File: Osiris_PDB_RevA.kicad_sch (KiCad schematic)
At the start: 69 parts, among them J1 MKDSP 25/2-15.00, J2 OSIRIS_I2C, J3 MKDSP 25/2-15.00, J4 XT60PW-F, Q1 ISC015N06NM5LF2, Q2 ISC015N06NM5LF2, Q3 BSC070N10NS5, U1 LTC4368HMS-1-PBF, U2 INA228AIDGSR, U3 LT3010EMS8E, U4 74AUP1G07GW, U5 LTC4359IMS8

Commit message: Update REV1.1 XT60 PDB and publish clean JLCPCB outputs
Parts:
- C17: value 470u 35V HYBRID -> 330u 50V HYBRID; MPN EEHZS1V471P -> EEHZL1H331P; Selection_Status Selected EEHZS1V471P G16; 10 mm diameter, 16.5 mm height. A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 -> Voltage rating increased to 50 V; same G16 footprint. Nomin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
- D5: value SMBJ24CA -> SMBJ18CA; MPN SMBJ24CA -> SMBJ18CA; Selection_Status SMBJ24CA retained for local ringing control. Clamp is not a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 -> Selected for confirmed 4S 16.8 V supply and 50 V C17. Clamp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
- J1, J3: value MKDSP 25/2-15.00 -> XT60PW-F; footprint PDB_Footprints:Connector_MKDSP25_2_15mm -> PDB_Footprints:AMASS_XT60PW-F_1x02_P7.20mm_Horizontal_EdgeMounted; symbol PDB_Symbols:Conn_01x02_Phoenix -> PDB_Symbols:XT60PW_F; MPN 1932588 -> XT60PW-F; Manufacturer Phoenix Contact -> AMASS; Selection_Status Drawing checked 2026-10-01: 15 mm pole pitch, 3.8 mm paired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 -> XT60PW-F rated 45 A, momentary 60 A with duration unspecifi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
- J4: footprint PDB_Footprints:AMASS_XT60PW-F_1x02_P7.20mm_Horizontal -> PDB_Footprints:AMASS_XT60PW-F_1x02_P7.20mm_Horizontal_EdgeMounted
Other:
- note added: "DEDICATED ESC POWER | 4S / XT60 PROTOTYPE / CURRENT TO BE QUALIFIED"
- note added: "J3 ESC OUTPUT ONLY. F2/D5/C17-C19 bypass the separate J4 avionics branch. XT60 prototype uses parallel ESC positive copper and ground return copper. J1 pack interface, fuse land pattern, copper, fault current and heating need verification."
- note added: "XT60 PROTOTYPE PCB: J1 input, J3 ESC output after F2, J4 Osiris avionics output after F1. Planning load: 50 A ESC + 5 A J1 avionics allowance; previous targets 60 A ESC continuous / 100 A for 30 s are NOT supported by XT60PW-F ratings. These currents are not yet qualified by the saved copper, terminals, fuse or pack connector."
- note removed: "DEDICATED ESC POWER | 4S / 60 A CONTINUOUS / 100 A FOR 30 s (PROVISIONAL)"
- note removed: "J3 ESC OUTPUT ONLY. F2/D5/C17-C19 bypass the separate J4 avionics branch. Phoenix lab PCB routes ESC positive on F.Cu and return through ground copper. J1 pack interface, fuse land pattern, copper, fault current and heating need verification."
- note removed: "PHOENIX LAB PCB: J1 input, J3 ESC output after F2, J4 Osiris avionics output after F1. Planning load: 50 A ESC + 5 A J1 avionics allowance; design targets 60 A ESC continuous / 100 A for 30 s. These currents are not yet qualified by the saved copper, terminals, fuse or pack connector."
- title: Osiris PDB - Phoenix lab board -> Osiris PDB - XT60 prototype
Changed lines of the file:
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@@
 	(paper "A3")
 	(title_block
-		(title "Osiris PDB - Phoenix lab board")
-		(date "2026-10-01")
-		(rev "A-P6-PROTOTYPE")
+		(title "Osiris PDB - XT60 prototype")
+		(date "2026-10-08")
+		(rev "1.1-XT60-PROTOTYPE")
 		(comment 1 "J1 common input; J3 ESC output; J4 protected Osiris avionics output")
-		(comment 2 "4-layer 2 oz prototype - physical qualification pending")
+		(comment 2 "4-layer 1 oz outer / 0.5 oz inner XT60 prototype - current qualification pending")
 	)
 	(text "STATUS / OPTIONAL PULL-UPS"
@@
 		)
 	)
-	(text "J3 ESC OUTPUT ONLY. F2/D5/C17-C19 bypass the separate J4 avionics branch.\nPhoenix lab PCB routes ESC positive on F.Cu and return through ground copper.\nJ1 pack interface, fuse land pattern, copper, fault current and heating need verification."
+	(text "J3 ESC OUTPUT ONLY. F2/D5/C17-C19 bypass the separate J4 avionics branch.\nXT60 prototype uses parallel ESC positive copper and ground return copper.\nJ1 pack interface, fuse land pattern, copper, fault current and heating need verification."
 		(exclude_from_sim no)
 		(at 255.27 97.79 0)
@@
 		)
 	)
-	(text "PHOENIX LAB PCB: J1 input, J3 ESC output after F2, J4 Osiris avionics output after F1.\nPlanning load: 50 A ESC + 5 A J1 avionics allowance; design targets 60 A ESC continuous / 100 A for 30 s.\nThese currents are not yet qualified by the saved copper, terminals, fuse or pack connector."
+	(text "XT60 PROTOTYPE PCB: J1 input, J3 ESC output after F2, J4 Osiris avionics output after F1.\nPlanning load: 50 A ESC + 5 A J1 avionics allowance; previous targets 60 A ESC continuous / 100 A for 30 s are NOT supported by XT60PW-F ratings.\nThese currents are not yet qualified by the saved copper, terminals, fuse or pack connector."
 		(exclude_from_sim no)
 		(at 20.32 276.86 0)
@@
 		)
 	)
-	(text "DEDICATED ESC POWER  |  4S / 60 A CONTINUOUS / 100 A FOR 30 s (PROVISIONAL)"
+	(text "DEDICATED ESC POWER  |  4S / XT60 PROTOTYPE / CURRENT TO BE QUALIFIED"
 		(exclude_from_sim no)
 		(at 255.27 91.44 0)
@@
 			)
 		)
-		(property "Value" "470u 35V HYBRID"
+		(property "Value" "330u 50V HYBRID"
 			(at 326.39 80.01 0)
 			(show_name no)
@@
 			)
 		)
-		(property "Datasheet" "${KIPRJMOD}/Datasheets/Panasonic_ZS.pdf"
+		(property "Datasheet" "${KIPRJMOD}/Datasheets/Panasonic_ZL.pdf"
 			(at 322.58 76.2 0)
 			(hide yes)
@@
 			)
 		)
-		(property "Description" "Local supplemental ESC capacitor: 470 uF, 35 V, hybrid, 11 mOhm ESR at 100 kHz, 4 Arms at 100 kHz/125 C. Preserve the ESC manufacturer-required capacitor at the ESC."
+		(property "Description" "Supplemental ESC capacitor, 330 uF 50 V hybrid, G16 10 x 16.5 mm; 12 mOhm at 100 kHz/20 C, 5 Arms at 100 kHz/125 C. Preserve ESC manufacturer-required capacitor at ESC."
 			(at 326.39 77.47 0)
 			(hide yes)
@@
 			)
 		)
-		(property "Selection_Status" "Selected EEHZS1V471P G16; 10 mm diameter, 16.5 mm height. Additional ESC-side capacitor and harness transient/ripple tests required."
+		(property "Selection_Status" "Voltage rating increased to 50 V; same G16 footprint. Nominal capacitance reduced from 470 to 330 uF. Validate installed harness transient/ripple and bulk capacitance."
 			(at 322.58 76.2 0)
 			(hide yes)
@@
 			)
 		)
-		(property "MPN" "EEHZS1V471P"
+		(property "MPN" "EEHZL1H331P"
 			(at 0 0 0)
 			(effects (font (size 1.27 1.27)) (hide yes))
@@
 			)
 		)
-		(property "Footprint" "PDB_Footprints:AMASS_XT60PW-F_1x02_P7.20mm_Horizontal"
+		(property "Footprint" "PDB_Footprints:AMASS_XT60PW-F_1x02_P7.20mm_Horizontal_EdgeMounted"
 			(at 388.62 35.56 0)
 			(hide yes)
@@
 	)
 	(symbol
-		(lib_id "PDB_Symbols:Conn_01x02_Phoenix")
+		(lib_id "PDB_Symbols:XT60PW_F")
 		(at 17.78 40.64 180)
 		(unit 1)
@@
 			)
 		)
-		(property "Value" "MKDSP 25/2-15.00"
+		(property "Value" "XT60PW-F"
 			(at 17.78 35.56 0)
 			(show_name no)
@@
 			)
 		)
-		(property "Footprint" "PDB_Footprints:Connector_MKDSP25_2_15mm"
+		(property "Footprint" "PDB_Footprints:AMASS_XT60PW-F_1x02_P7.20mm_Horizontal_EdgeMounted"
 			(at 17.78 40.64 0)
 			(hide yes)
@@
 			)
 		)
-		(property "Datasheet" "https://www.phoenixcontact.com/en-ca/products/printed-circuit-board-terminal-mkdsp-25-2-1500-1932588"
+		(property "Datasheet" "${KIPRJMOD}/Datasheets/AMASS_XT60PW-F.pdf"
 			(at 17.78 40.64 0)
 			(hide yes)
@@
 			)
 		)
-		(property "Description" "4S battery input; pin 1 GND, pin 2 VBAT_RAW. Phoenix Contact 1932588 terminal; footprint and assembly require verification."
+		(property "Description" "AMASS board-mounted XT60PW-F. Pin 1 GND, pin 2 positive."
 			(at 17.78 35.56 0)
 			(hide yes)
@@
 			)
 		)
-		(property "Selection_Status" "Drawing checked 2026-10-01: 15 mm pole pitch, 3.8 mm paired pins, 12.5 mm row pitch, 1.6 mm holes. 125 A part rating is conditional on conductor and temperature; assembly and harness qualification required."
+		(property "Selection_Status" "XT60PW-F rated 45 A, momentary 60 A with duration unspecified. Old 60 A continuous / 100 A burst board targets not supported."
 			(at 17.78 40.64 0)
 			(hide yes)
@@
 			)
 		)
-		(property "Manufacturer" "Phoenix Contact"
+		(property "Manufacturer" "AMASS"
 			(at 17.78 40.64 0)
 			(hide yes)
@@
 			)
 		)
-		(property "MPN" "1932588"
+		(property "MPN" "XT60PW-F"
 			(at 17.78 40.64 0)
 			(hide yes)
@@
 		(in_pos_files yes)
 		(dnp no)
-		(property "MPN" "SMBJ24CA"
+		(property "MPN" "SMBJ18CA"
 			(at 300.99 78.74 0)
 			(hide yes)
@@
 			)
 		)
-		(property "Value" "SMBJ24CA"
+		(property "Value" "SMBJ18CA"
 			(at 304.8 80.01 90)
 			(show_name no)
@@
 			)
 		)
-		(property "Description" "Bidirectional 24 V TVS candidate for local ESC connector ringing control; validate pulse energy and clamp voltage on the installed harness."
+		(property "Description" "4S ESC transient suppressor: 18 V standoff; 29.2 V clamp at 20.6 A 10/1000 us; 38.0 V at 103 A 8/20 us. Same SMB footprint."
 			(at 304.8 77.47 90)
 			(hide yes)
@@
 			)
 		)
-		(property "Selection_Status" "SMBJ24CA retained for local ringing control. Clamp is not a 35 V ceiling; verify installed 4S harness waveforms and pulse energy."
+		(property "Selection_Status" "Selected for confirmed 4S 16.8 V supply and 50 V C17. Clamp and pulse energy depend on installed harness and temperature; not a sustained overvoltage regulator."
 			(at 300.99 76.2 0)
 			(hide yes)
@@
 	)
 	(symbol
-		(lib_id "PDB_Symbols:Conn_01x02_Phoenix")
+		(lib_id "PDB_Symbols:XT60PW_F")
 		(at 388.62 72.39 0)
 		(unit 1)
@@
 			)
 		)
-		(property "Value" "MKDSP 25/2-15.00"
+		(property "Value" "XT60PW-F"
 			(at 388.62 67.31 0)
 			(show_name no)
@@
 			)
 		)
-		(property "Footprint" "PDB_Footprints:Connector_MKDSP25_2_15mm"
+		(property "Footprint" "PDB_Footprints:AMASS_XT60PW-F_1x02_P7.20mm_Horizontal_EdgeMounted"
 			(at 388.62 50.8 0)
 			(hide yes)
@@
 			)
 		)
-		(property "Datasheet" "https://www.phoenixcontact.com/en-ca/products/printed-circuit-board-terminal-mkdsp-25-2-1500-1932588"
+		(property "Datasheet" "${KIPRJMOD}/Datasheets/AMASS_XT60PW-F.pdf"
 			(at 388.62 50.8 0)
 			(hide yes)
@@
 			)
 		)
-		(property "Description" "Dedicated ESC output after F2; pin 1 GND, pin 2 ESC_VBAT. Phoenix Contact 1932588 terminal; footprint and assembly require verification."
+		(property "Description" "AMASS board-mounted XT60PW-F. Pin 1 GND, pin 2 positive."
 			(at 388.62 45.72 0)
 			(hide yes)
@@
 			)
 		)
-		(property "Selection_Status" "Drawing checked 2026-10-01: 15 mm pole pitch, 3.8 mm paired pins, 12.5 mm row pitch, 1.6 mm holes. 125 A part rating is conditional on conductor and temperature; assembly and harness qualification required."
+		(property "Selection_Status" "XT60PW-F rated 45 A, momentary 60 A with duration unspecified. Old 60 A continuous / 100 A burst board targets not supported."
 			(at 388.62 50.8 0)
 			(hide yes)
@@
 			)
 		)
-		(property "Manufacturer" "Phoenix Contact"
+		(property "Manufacturer" "AMASS"
 			(at 388.62 50.8 0)
 			(hide yes)
@@
 			)
 		)
-		(property "MPN" "1932588"
+		(property "MPN" "XT60PW-F"
 			(at 388.62 50.8 0)
 			(hide yes)

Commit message: Use stocked passive alternatives and refresh REV1.1 procurement outputs
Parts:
- C18: MPN C2012X7R1H105K125AB -> CC0805KKX7R9BB105; Manufacturer TDK -> YAGEO; Selection_Status Prototype selection: 1 uF 50 V X7R 10%, 0805. Nominal speci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 -> Selected; verified package and ratings; LCSC stock snapshot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
- C19: MPN C0805C104K5RACTU -> CC0805KRX7R9BB104; Manufacturer KEMET -> YAGEO; Selection_Status Prototype selection: 100 nF 50 V X7R 10%, 0805. Nominal spe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 -> Selected; verified package and ratings; LCSC stock snapshot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
- C2: MPN C2012X7R1H105K125AB -> CC0805KKX7R9BB105; Manufacturer TDK -> YAGEO; Selection_Status Nominal specification verified; DC-bias and circuit validat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 -> Selected; verified package and ratings; LCSC stock snapshot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
- R10: MPN RC0805FR-074K7L -> 0805W8F4701T5E; Manufacturer YAGEO -> UNI-ROYAL; Selection_Status Package assigned; MPN and power/tolerance validation pending -> Selected; verified package and ratings; LCSC stock snapshot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
- R12: MPN RC0805FR-071KL -> 0805W8F1001T5E; Manufacturer YAGEO -> UNI-ROYAL; Selection_Status A-P2 U3 feedback network; layout and assembled transient ve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 -> Selected; verified package and ratings; LCSC stock snapshot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
- R15, R16: MPN RC0805FR-0710KL -> 0805W8F1002T5E; Manufacturer YAGEO -> UNI-ROYAL; Selection_Status Rev-B candidate; MPN pending distributor check -> Selected; verified package and ratings; LCSC stock snapshot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
- R21: MPN RC0805FR-07100RL -> 0805W8F1000T5E; Manufacturer Yageo -> UNI-ROYAL; Selection_Status Selected: VBUS filter with C14. Allow 1 ms settling before 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 -> Selected; verified package and ratings; LCSC stock snapshot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
- R3: MPN RC0805FR-072ML -> 0805W8F2004T5E; Manufacturer YAGEO -> UNI-ROYAL; Selection_Status Package assigned; MPN and power/tolerance validation pending -> Selected; verified package and ratings; LCSC stock snapshot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
- R4: MPN RC0805FR-0722KL -> 0805W8F2202T5E; Manufacturer YAGEO -> UNI-ROYAL; Selection_Status U1 GATE directly drives Q1/Q2. R4 is in series with C1 to g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 -> Selected; verified package and ratings; LCSC stock snapshot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
- R6: MPN RC0805FR-07680KL -> 0805W8F6803T5E; Manufacturer YAGEO -> UNI-ROYAL; Selection_Status Package assigned; MPN and power/tolerance validation pending -> Selected; verified package and ratings; LCSC stock snapshot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
- R7: MPN RC0805FR-07200KL -> 0805W8F2003T5E; Manufacturer YAGEO -> UNI-ROYAL; Selection_Status Package assigned; MPN and power/tolerance validation pending -> Selected; verified package and ratings; LCSC stock snapshot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
- R8, R9: MPN RC0805FR-0710RL -> 0805W8F100JT5E; Manufacturer YAGEO -> UNI-ROYAL; Selection_Status Package assigned; MPN and power/tolerance validation pending -> Selected; verified package and ratings; LCSC stock snapshot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

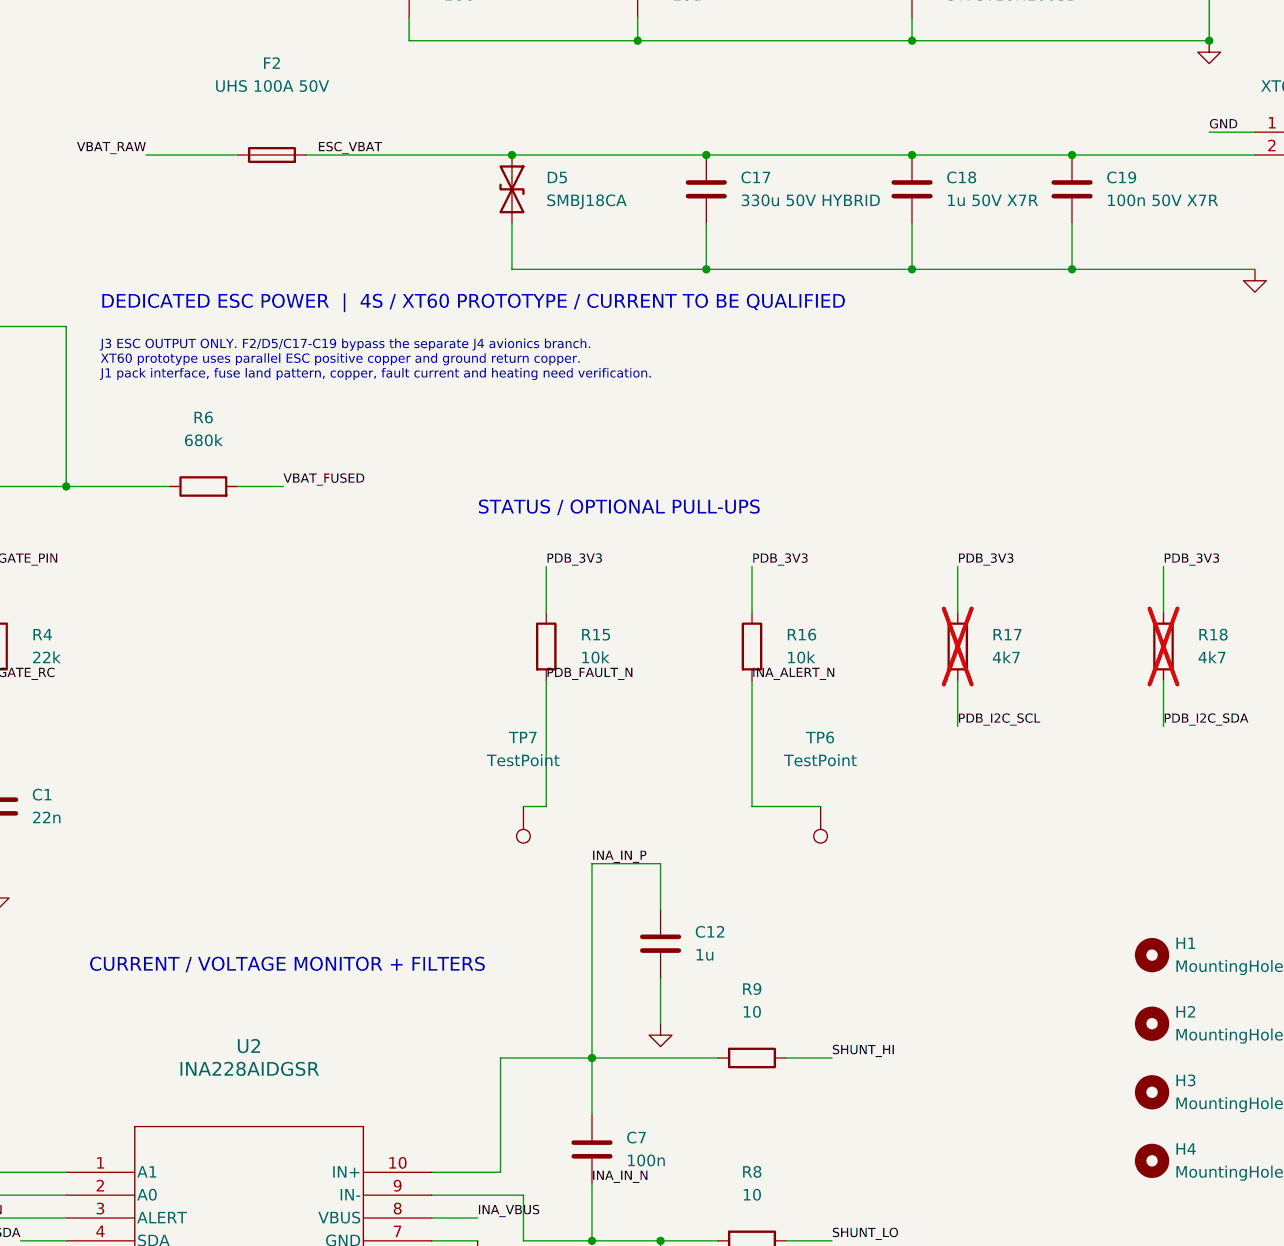
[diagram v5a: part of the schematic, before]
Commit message: Update INA238 telemetry, ESC capacitor bank and procurement outputs
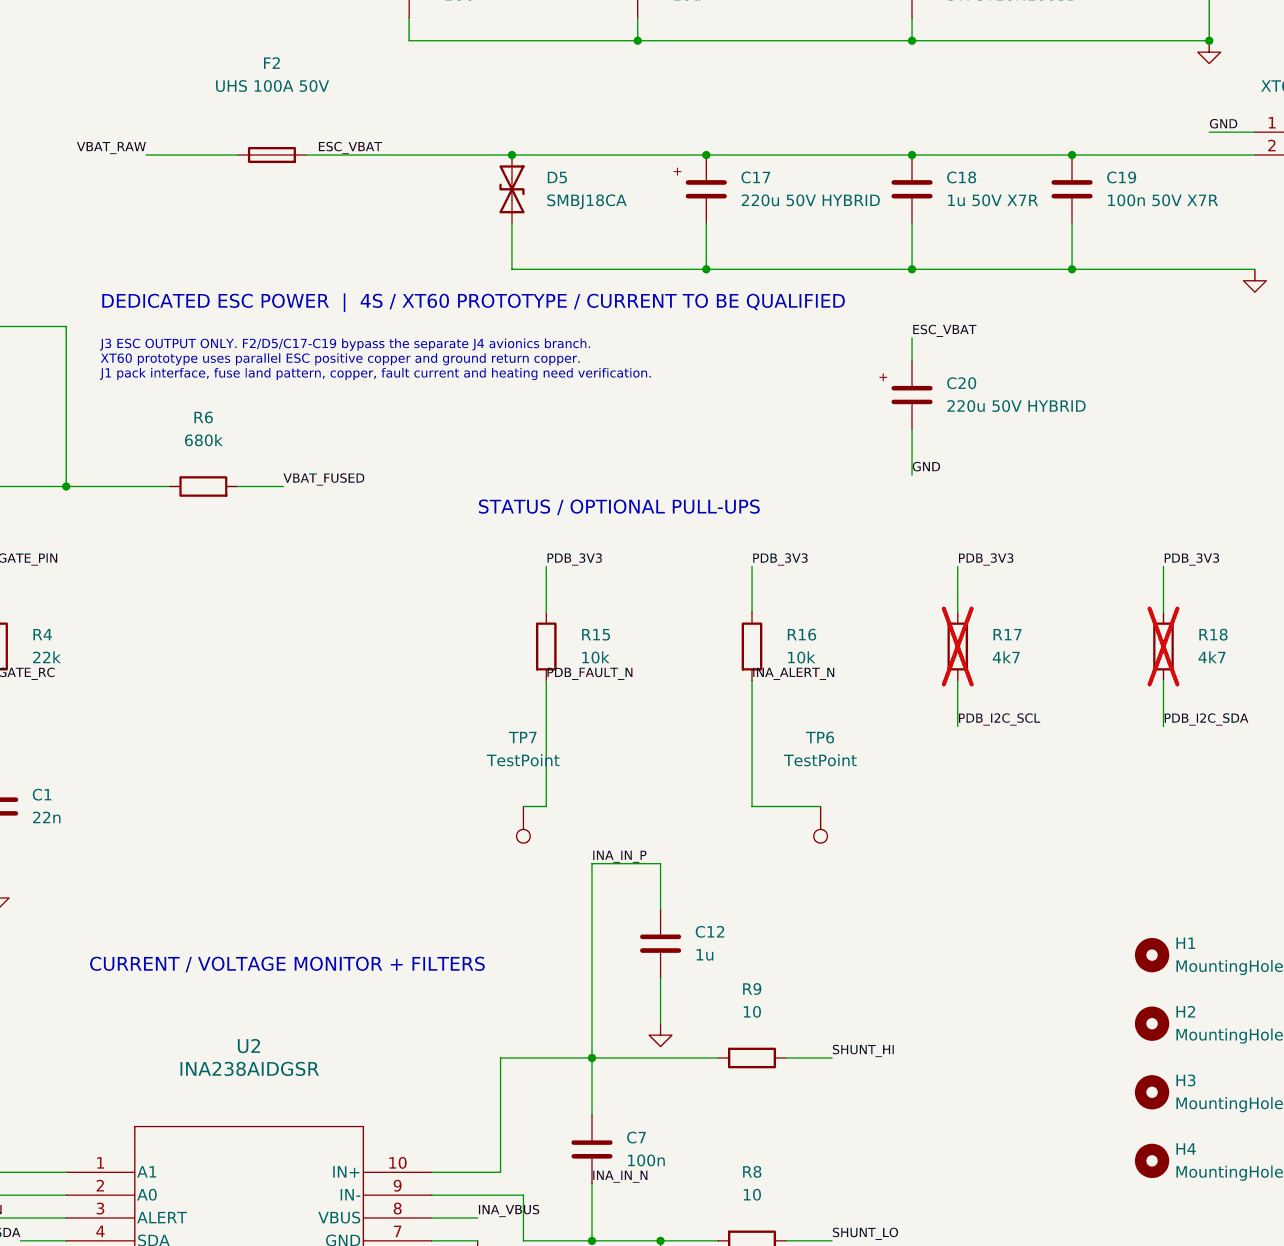
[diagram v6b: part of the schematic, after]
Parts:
- added C20: 220u 50V HYBRID, PDB_Footprints:CP_Elec_Panasonic_G16_10x16.5_ZS, symbol PDB_Symbols:CP_Elec_Panasonic
- C10, C3, C5, C8: MPN C0603C104K4RACTU -> CC0603KRX7R9BB104; Manufacturer KEMET -> YAGEO
- C11, C12, C13, C14, C15, C16: MPN B32529C0105J189 -> B32529C0105J000
- C17: value 330u 50V HYBRID -> 220u 50V HYBRID; footprint PDB_Footprints:CP_Elec_Panasonic_G16_10x16.5 -> PDB_Footprints:CP_Elec_Panasonic_G16_10x16.5_ZS; MPN EEHZL1H331P -> EEHZS1H221P; Selection_Status Voltage rating increased to 50 V; same G16 footprint. Nomin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 -> Two-part ESC capacitor bank. Verify installed transient, in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
- C4, C9: MPN C3216X7R1H106K160AC -> CL31B106KBHNNNE; Manufacturer TDK -> Samsung Electro-Mechanics
- C6: MPN C2012X7R1A106K125AC -> CL21B106KAYQNNE; Manufacturer TDK -> Samsung Electro-Mechanics
- C7: MPN C1608X7R1H104K080AA -> CC0603KRX7R9BB104; Manufacturer TDK -> YAGEO
- R1: MPN RC0805FR-07237KL -> FRC0805F2373TS; Manufacturer YAGEO -> FOJAN
- R11: MPN RC0805FR-071K58L -> PTFR0805B1K58P9; Manufacturer YAGEO -> RESI
- R13: MPN RC0805FR-0754K9L -> 0805W8F5492T5E; Manufacturer YAGEO -> UNI-ROYAL
- R14: MPN RC0805JR-0722ML -> FRG0805J226TS; Manufacturer YAGEO -> FOJAN
- R19: MPN CRCW25121001FKEGHP -> CRCW25121K00FKEGHP
- R2: MPN RC0805FR-0711K8L -> FRC0805F1182TS; Manufacturer YAGEO -> FOJAN
- U1: MPN LTC4368HMS-1#TRPBF -> LTC4368HMS-1#WTRPBF
- U2: value INA228AIDGSR -> INA238AIDGSR; symbol PDB_Symbols:INA228AIDGSR -> PDB_Symbols:INA238AIDGSR; MPN INA228AIDGSR -> INA238AIDGSR; Selection_Status (none) -> INA238 substitution: 16-bit resolution, 0x40 address; not f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
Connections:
- net ESC_VBAT: now also C20.1
- net GND: now also C20.2

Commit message: Update JLC sourcing BOM and five-board procurement workbooks
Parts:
- D1, D4: Manufacturer Bourns -> RUILON
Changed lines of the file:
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@@
 			)
 		)
-		(property "Datasheet" "${KIPRJMOD}/Datasheets/Bourns_SMAJ_TVS.pdf"
+		(property "Datasheet" "https://www.lcsc.com/product-detail/C28092.html"
 			(at 142.24 55.88 0)
 			(hide yes)
@@
 			)
 		)
-		(property "Manufacturer" "Bourns"
+		(property "Manufacturer" "RUILON"
 			(at 142.24 55.88 0)
 			(hide yes)
@@
 			)
 		)
-		(property "Datasheet" "${KIPRJMOD}/Datasheets/Bourns_SMAJ_TVS.pdf"
+		(property "Datasheet" "https://www.lcsc.com/product-detail/C28092.html"
 			(at 50.8 99.06 0)
 			(hide yes)
@@
 			)
 		)
-		(property "Manufacturer" "Bourns"
+		(property "Manufacturer" "RUILON"
 			(at 50.8 99.06 0)
 			(hide yes)
@@
 			)
 		)
-		(property "Datasheet" "https://www.digikey.com/en/products/detail/vishay-dale/CRCW25121K00FKEGHP/2222092"
+		(property "Datasheet" "https://www.digikey.com/en/products/detail/vishay-dale/CRCW25121K00FKEGHP/2222612"
 			(at 115.57 115.57 0)
 			(hide yes)
